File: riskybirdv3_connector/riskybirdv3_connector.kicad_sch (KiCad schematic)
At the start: 92 parts, among them J1 USB_C_Receptacle_USB2.0_16P, J2 USB_C_Receptacle_USB2.0_16P, J3 Conn_02x10_Odd_Even, U1 AP2112K-3.3, U15 FT2232HL-REEL, U2 AP2112K-3.3, U9 FT2232HL-REEL, Y2 f, Y3 f

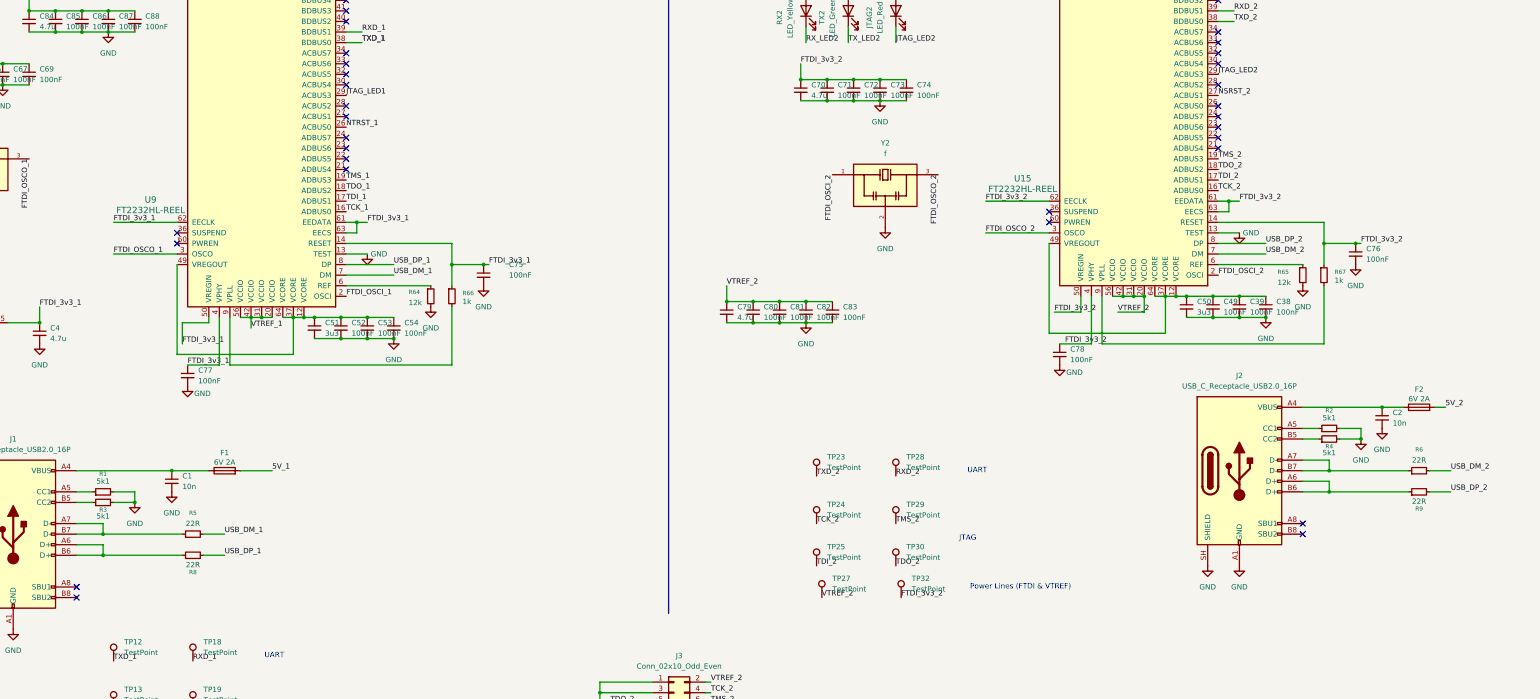
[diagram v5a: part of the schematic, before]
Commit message: riskybirdv3 connector (programmer): VPLL/VPHY ferrites + 93LC66C EEPROM + design-rule sync
Programmer/connector board respin updates.

Schematic (riskybirdv3_connector.kicad_sch):
- Added VPLL/VPHY supply ferrites FB2-FB5 for FTDI PLL/PHY rail filtering.
- Removed the 22 ohm USB series resistors (direct USB D+/D- routing).
- Wired 93LC66C EEPROM (U3) for FTDI USB descriptor/config storage.
- LCSC part sync.

PCB (riskybirdv3_connector.kicad_pcb):
- Layout updated to match the ferrite/EEPROM/USB schematic changes.

Design rules:
- riskybirdv3_connector.kicad_dru + JLCPCB.kicad_dru synced from the
  base board's rule set.
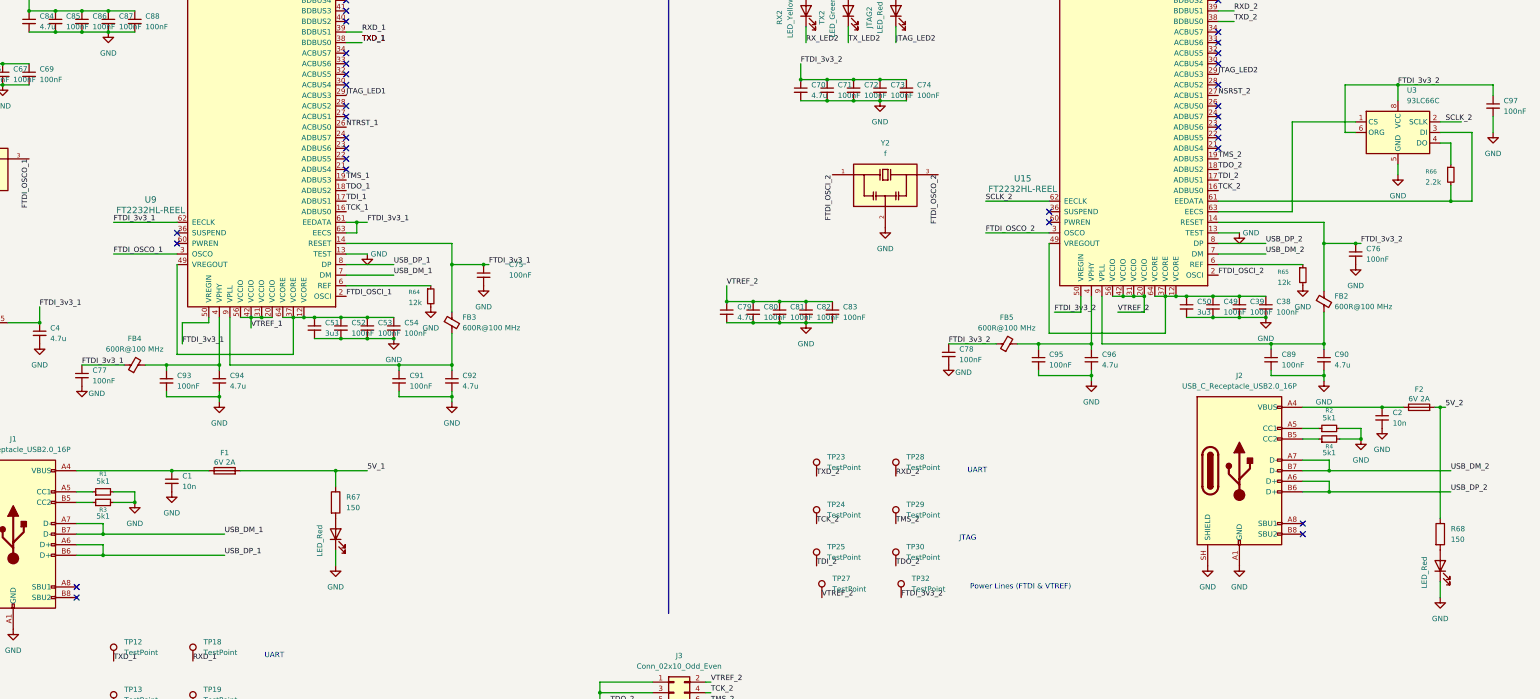
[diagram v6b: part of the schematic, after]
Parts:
- removed R5, R6, R8, R9: 22R, Resistor_SMD:R_0201_0603Metric, symbol Device:R_Small
- removed R67: 1k, Resistor_SMD:R_0201_0603Metric, symbol Device:R_Small
- added C89, C91, C93, C95, C97: 100nF, Capacitor_SMD:C_0201_0603Metric, symbol Device:C_Small
- added C90, C92, C94, C96: 4.7u, Capacitor_SMD:C_0402_1005Metric, symbol Device:C_Small
- added FB2, FB3, FB4, FB5: 600R@100 MHz, Inductor_SMD:L_0603_1608Metric, symbol Device:FerriteBead_Small
- added JTAG3, JTAG4: LED_Red, LED_SMD:LED_0402_1005Metric, symbol Device:LED
- added R67, R68: 150, Resistor_SMD:R_0201_0603Metric, symbol Device:R
- added U3: 93LC66C, Package_SO:MSOP-8_3x3mm_P0.65mm, symbol Memory_EEPROM:93LCxxB
- R10, R7: now left out of the parts list
- R66: value 1k -> 2.2k; LCSC Part C270365 -> C270363; MPN 0201WMF1001TEE -> 0201WMF1202TEE
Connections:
- net 5V_1: now also R67.1
- net 5V_2: now also R68.1
- net FTDI_3v3_1: now also FB3.1, FB4.1; no longer R66.1, U9.4 (VPHY)
- net FTDI_3v3_2: now also C97.1, FB2.1, FB5.1, U3.6 (ORG), U3.8 (VCC); no longer U15.4 (VPHY), U15.61 (EEDATA), U15.62 (EECLK), U15.63 (EECS)
- net GND: now also C89.2, C90.2, C91.2, C92.2, C93.2, C94.2, C95.2, C96.2, C97.2, JTAG3.1 (K), JTAG4.1 (K), U3.5 (GND)
- net USB_DM_1: now also J1.A7 (D-), J1.B7 (D-)
- net USB_DM_2: now also J2.A7 (D-), J2.B7 (D-)
- net USB_DP_1: now also J1.A6 (D+), J1.B6 (D+)
- net USB_DP_2: now also J2.A6 (D+), J2.B6 (D+)
- net at R66.2: now also U15.61 (EEDATA), U3.3 (DI); no longer U9.9 (VPLL)
- net at U15.9 (VPLL): now also C89.1, C90.1, FB2.2
- new net: JTAG3.2 (A), R67.2
- new net: R66.1, U3.4 (DO)
- new net: C93.1, C94.1, FB4.2, U9.4 (VPHY)
- new net: C91.1, C92.1, FB3.2, U9.9 (VPLL)
- new net: JTAG4.2 (A), R68.2
- new net: C95.1, C96.1, FB5.2, U15.4 (VPHY)
- new net: U15.63 (EECS), U3.1 (CS)
- new net SCLK_2: U15.62 (EECLK), U3.2 (SCLK)
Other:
- moved on the sheet: C77, C78
